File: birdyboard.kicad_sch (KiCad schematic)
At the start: 12 parts, among them P0 24V Input Screw Terminal, U0 TMC2208_SILENTSTEPSTICK, U1 TMC2208_SILENTSTEPSTICK, U2 TMC2208_SILENTSTEPSTICK, U3 TMC2208_SILENTSTEPSTICK, U5 Pico, U6 SN74CBT3253 MUX/DEMUX

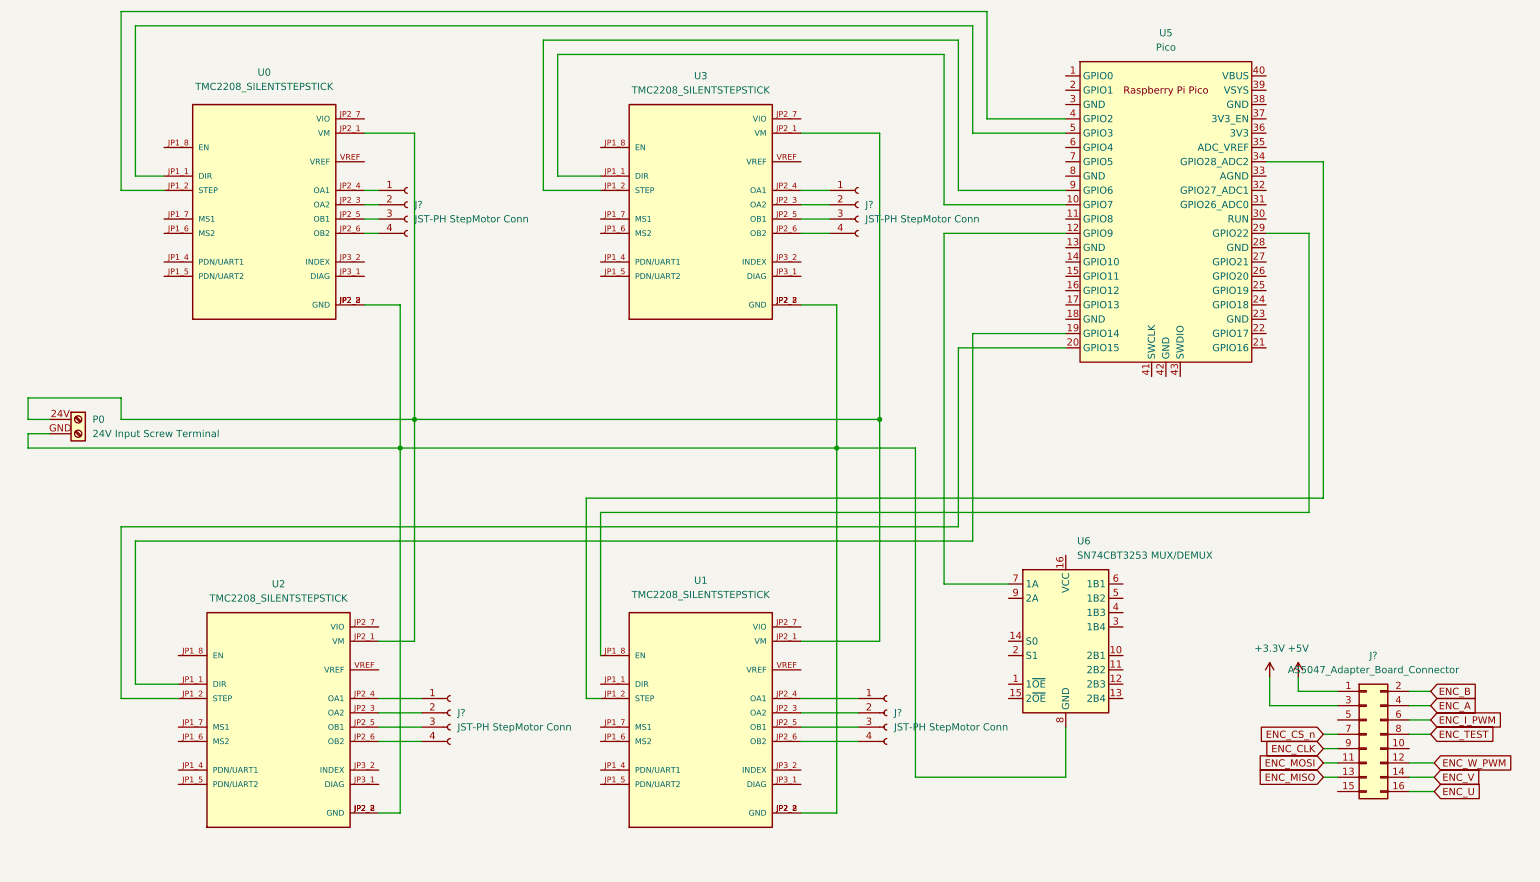
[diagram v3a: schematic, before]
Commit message: add netlabels and power ports
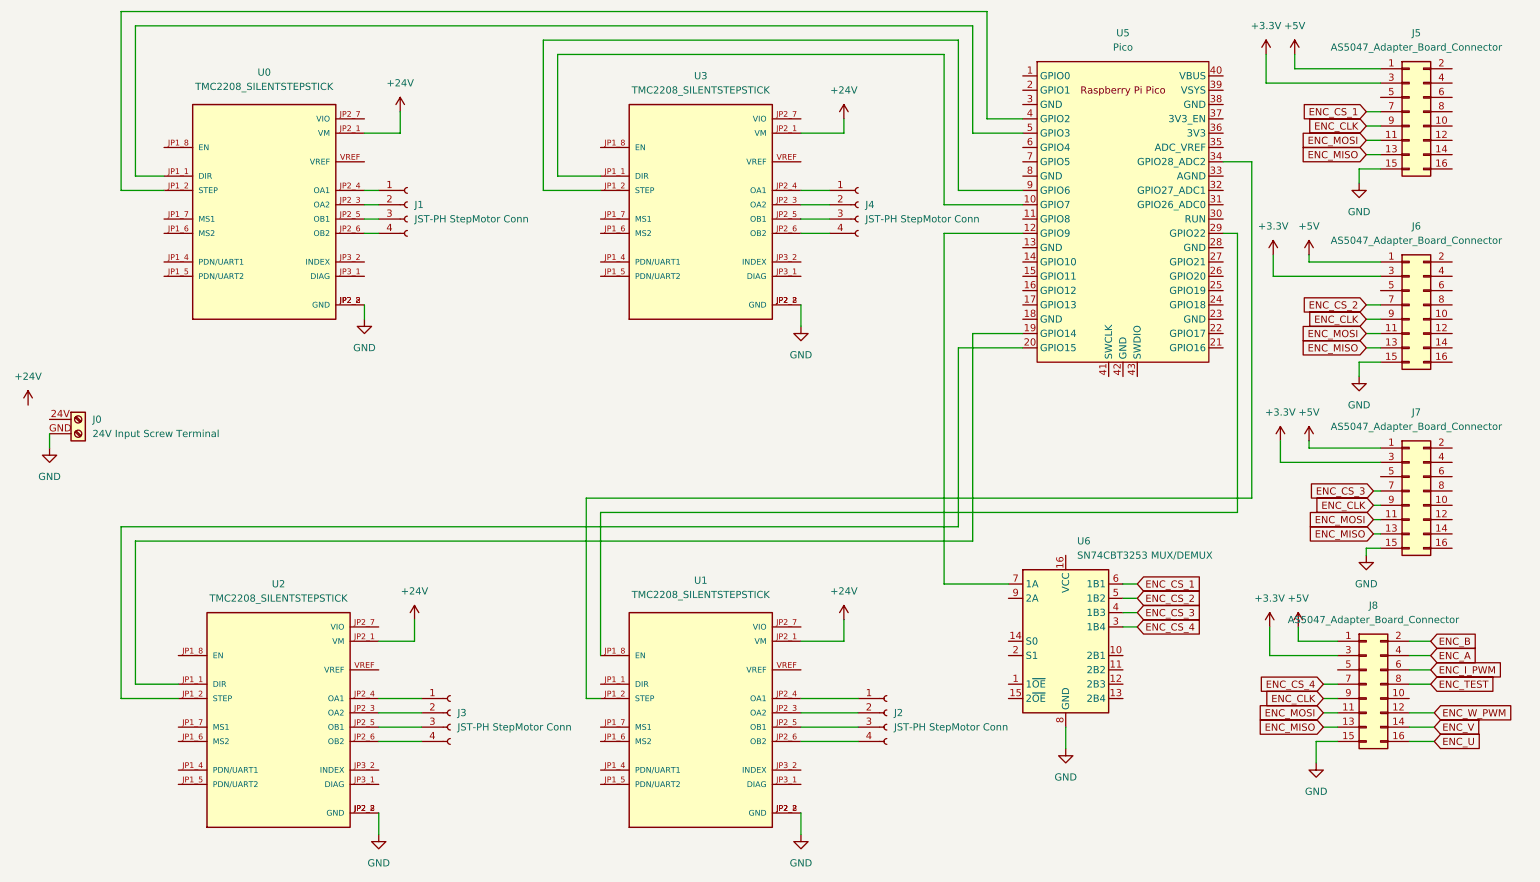
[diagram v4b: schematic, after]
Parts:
- added J5, J6, J7: AS5047_Adapter_Board_Connector, symbol Connector_Generic:Conn_02x08_Odd_Even
- gave numbers to parts that had none: 5
- renumbered P0 to J0
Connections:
- net ENC_CS_n is gone; now on net ENC_CS_4: J8.7 (Pin_7)
- net +5V: now also J5.1 (Pin_1), J6.1 (Pin_1), J7.1 (Pin_1)
- net ENC_CLK: now also J5.9 (Pin_9), J6.9 (Pin_9), J7.9 (Pin_9)
- net ENC_MISO: now also J5.13 (Pin_13), J6.13 (Pin_13), J7.13 (Pin_13)
- net ENC_MOSI: now also J5.11 (Pin_11), J6.11 (Pin_11), J7.11 (Pin_11)
- net +24V: now reaches U0.JP2_1 (VM), U1.JP2_1 (VM), U2.JP2_1 (VM), U3.JP2_1 (VM)
- net +24V: no longer J0.24V (Pin_1)
- net GND: now reaches J0.GND (Pin_2), U0.JP2_2 (GND), U0.JP2_8 (GND), U1.JP2_2 (GND), U1.JP2_8 (GND), U2.JP2_2 (GND), U2.JP2_8 (GND), U3.JP2_2 (GND), U3.JP2_8 (GND), U6.8 (GND)
- net GND: now also J8.15 (Pin_15), J5.15 (Pin_15), J6.15 (Pin_15), J7.15 (Pin_15)
- net ENC_CS_4: now reaches U6.3 (1B4)
- net ENC_CS_3: now reaches U6.4 (1B3)
- net ENC_CS_3: now also J7.7 (Pin_7)
- net ENC_CS_2: now reaches U6.5 (1B2)
- net ENC_CS_2: now also J6.7 (Pin_7)
- net ENC_CS_1: now reaches U6.6 (1B1)
- net ENC_CS_1: now also J5.7 (Pin_7)
- new net +3.3V: J5.3 (Pin_3), J6.3 (Pin_3), J7.3 (Pin_3)
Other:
- title: (none) -> BirdyBoard
- moved on the sheet: J8, U5

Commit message: fix small mistake
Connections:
- net at U5.29 (GPIO22): now also U1.JP1_1 (DIR); no longer U1.JP1_8 (EN)
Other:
- moved on the sheet: U1
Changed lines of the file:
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@@
     (stroke (width 0) (type default) (color 0 0 0 0))
   )
-  (wire (pts (xy 157.48 149.86) (xy 167.64 149.86))
+  (wire (pts (xy 160.02 149.86) (xy 167.64 149.86))
     (stroke (width 0) (type default) (color 0 0 0 0))
   )
@@
     (stroke (width 0) (type default) (color 0 0 0 0))
   )
+  (wire (pts (xy 121.92 142.24) (xy 124.46 142.24))
+    (stroke (width 0) (type default) (color 0 0 0 0))
+  )
   (wire (pts (xy 165.1 44.45) (xy 165.1 41.91))
     (stroke (width 0) (type default) (color 0 0 0 0))
@@
     (stroke (width 0) (type default) (color 0 0 0 0))
   )
-  (wire (pts (xy 121.92 137.16) (xy 121.92 111.76))
-    (stroke (width 0) (type default) (color 0 0 0 0))
-  )
   (wire (pts (xy 232.41 49.53) (xy 237.49 49.53))
     (stroke (width 0) (type default) (color 0 0 0 0))
   )
-  (wire (pts (xy 157.48 144.78) (xy 167.64 144.78))
+  (wire (pts (xy 160.02 144.78) (xy 167.64 144.78))
     (stroke (width 0) (type default) (color 0 0 0 0))
   )
@@
     (stroke (width 0) (type default) (color 0 0 0 0))
   )
-  (wire (pts (xy 157.48 152.4) (xy 167.64 152.4))
+  (wire (pts (xy 160.02 152.4) (xy 167.64 152.4))
     (stroke (width 0) (type default) (color 0 0 0 0))
   )
@@
     (stroke (width 0) (type default) (color 0 0 0 0))
   )
-  (wire (pts (xy 157.48 147.32) (xy 167.64 147.32))
+  (wire (pts (xy 160.02 147.32) (xy 167.64 147.32))
     (stroke (width 0) (type default) (color 0 0 0 0))
   )
@@
     (stroke (width 0) (type default) (color 0 0 0 0))
   )
-  (wire (pts (xy 157.48 165.1) (xy 157.48 168.91))
+  (wire (pts (xy 160.02 165.1) (xy 157.48 168.91))
     (stroke (width 0) (type default) (color 0 0 0 0))
   )
@@
     (stroke (width 0) (type default) (color 0 0 0 0))
   )
-  (wire (pts (xy 119.38 144.78) (xy 121.92 144.78))
+  (wire (pts (xy 119.38 144.78) (xy 124.46 144.78))
     (stroke (width 0) (type default) (color 0 0 0 0))
   )
@@
     (stroke (width 0) (type default) (color 0 0 0 0))
   )
-  (wire (pts (xy 157.48 134.62) (xy 165.1 134.62))
+  (wire (pts (xy 160.02 134.62) (xy 165.1 134.62))
     (stroke (width 0) (type default) (color 0 0 0 0))
   )
@@
   )
   (wire (pts (xy 250.19 147.32) (xy 252.73 147.32))
+    (stroke (width 0) (type default) (color 0 0 0 0))
+  )
+  (wire (pts (xy 121.92 111.76) (xy 121.92 142.24))
     (stroke (width 0) (type default) (color 0 0 0 0))
   )
@@
     (pin "1")
   )
-  (symbol (lib_id "birdyboard_library:TMC2208_SILENTSTEPSTICK") (at 139.7 147.32 0) (unit 1)
-    (in_bom yes) (on_board yes) (fields_autoplaced)
-    (property "Reference" "U1" (id 0) (at 139.7 123.825 0))
-    (property "Value" "TMC2208_SILENTSTEPSTICK" (id 1) (at 139.7 126.365 0))
-    (property "Footprint" "birdyboard:TMC2208_SILENTSTEPSTICK" (id 2) (at 139.7 147.32 0)
+  (symbol (lib_id "birdyboard_library:TMC2208_SILENTSTEPSTICK") (at 142.24 147.32 0) (unit 1)
+    (in_bom yes) (on_board yes) (fields_autoplaced)
+    (property "Reference" "U1" (id 0) (at 142.24 123.825 0))
+    (property "Value" "TMC2208_SILENTSTEPSTICK" (id 1) (at 142.24 126.365 0))
+    (property "Footprint" "birdyboard:TMC2208_SILENTSTEPSTICK" (id 2) (at 142.24 147.32 0)
       (effects (font (size 1.27 1.27)) (justify left bottom) hide)
     )
-    (property "Datasheet" "" (id 3) (at 139.7 147.32 0)
+    (property "Datasheet" "" (id 3) (at 142.24 147.32 0)
       (effects (font (size 1.27 1.27)) (justify left bottom) hide)
     )
-    (property "MANUFACTURER" "Trinamic Motion" (id 4) (at 139.7 147.32 0)
+    (property "MANUFACTURER" "Trinamic Motion" (id 4) (at 142.24 147.32 0)
       (effects (font (size 1.27 1.27)) (justify left bottom) hide)
     )

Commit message: add more netlabels
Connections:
- net DIR_0: now reaches U3.JP1_1 (DIR)
- net DIR_0: now also U5.9 (GPIO6); no longer U5.10 (GPIO7)
- net STEP_0: now reaches U3.JP1_2 (STEP)
- net STEP_0: now also U5.10 (GPIO7); no longer U5.9 (GPIO6)
- net DIR_1: now reaches U2.JP1_1 (DIR), U5.19 (GPIO14)
- net STEP_1: now reaches U2.JP1_2 (STEP), U5.20 (GPIO15)
- net at U5.12 (GPIO9): no longer U6.7 (1A)
- net DIR_2: now reaches U1.JP1_1 (DIR), U5.29 (GPIO22)
- net STEP_2: now reaches U1.JP1_2 (STEP), U5.34 (GPIO28_ADC2)
- net DIR_3: now reaches U5.4 (GPIO2)
- net DIR_3: now also U0.JP1_1 (DIR); no longer U0.JP1_2 (STEP)
- net STEP_3: now reaches U5.5 (GPIO3)
- net STEP_3: now also U0.JP1_2 (STEP); no longer U0.JP1_1 (DIR)
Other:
- moved on the sheet: J6, U5
